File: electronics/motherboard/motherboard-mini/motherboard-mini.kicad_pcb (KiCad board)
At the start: 2 copper layers, 106.6 x 156.6 mm, 167 parts, among them J1 JTAG, J10 CONUFL001-SMD-T, J11 SIM8060-6-0-14-00-A, J12 JTAG, J2 ST1W008S4AR1500, J3 3020-14-0300-00, J5 USB4070-30-C_REVC5, J8 SOLAR_CONN, Q1 MMDT3904, Q2 BC847, Q3 BSS214NW, Q4 BC847, Q5 BC847, SW1 BOOT, SW2 RESET, SW3 PROG_BTN, SW4 CAT_M1_RST, U1 CP2102N-Axx-xQFN28, U10 TPS22967DSGR, U11 SARA-R410M-02B, U12 AOZ8904CIL, U13 TXB0104PW, U14 TCA9534, U2 ESP32-WROOM-32E_(16MB), U3 INA219BxD, U4 LT3652IMSE, U5 MCP73832-2-OT, U6 INA219BxD, U7 MIC2288YD5-TR, U8 XC6215B332MR-G, U9 NCP718xSN500, Y1 32.768KHz

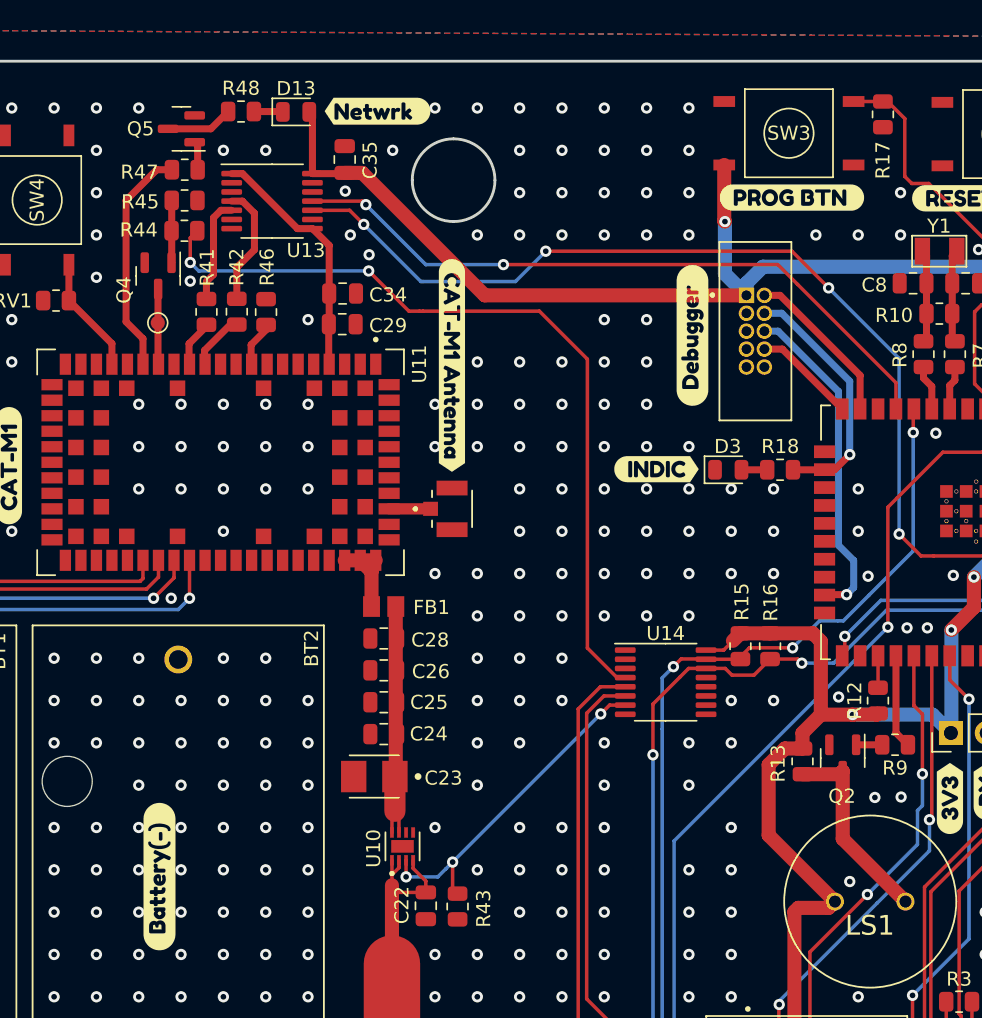
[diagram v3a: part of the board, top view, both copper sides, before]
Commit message: added cat-m1 basic interface
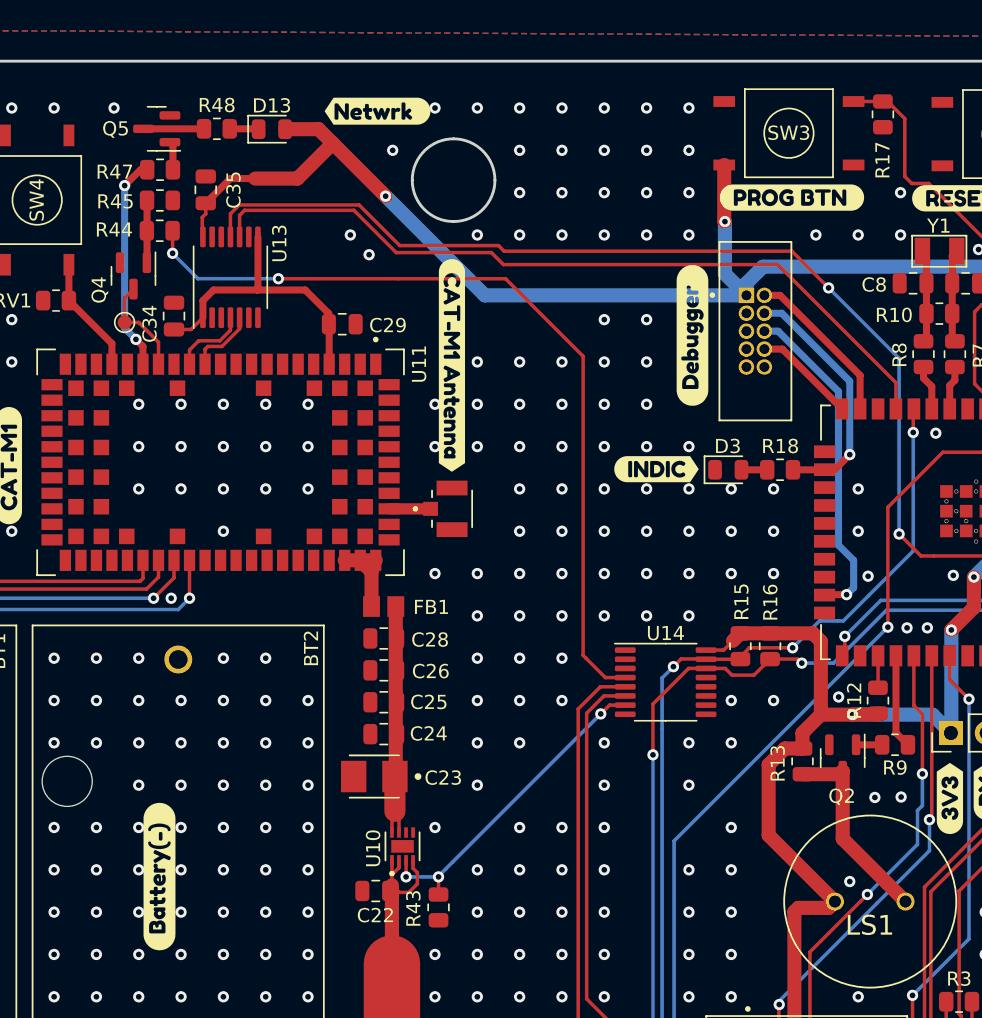
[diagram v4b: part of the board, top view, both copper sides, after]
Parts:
- removed R41, R42, R46: 0, Resistor_SMD:R_0805_2012Metric
- R28: value 27K -> 10K
- R29: value 53.6K -> 21K
- R39: value 43.3K -> 47K
- R40: value 5K -> 4.7K
- moved C34 12.1 mm to (65.5, 44.8), turned to 90 degrees
- moved C35 10.1 mm to (67.8, 35.8)
- moved U13 6.15 mm to (69.5, 42.0), turned to 90 degrees
- moved C22 3.70 mm to (79.8, 85.5), turned to 180 degrees
- moved TP4 2.35 mm to (62.0, 45.2)
- moved D13 2.11 mm to (72.4, 31.5)
- moved R48 2.11 mm to (68.5, 31.5)
- moved Q4 1.75 mm to (62.6, 41.9)
- moved Q5 1.75 mm to (64.3, 31.5)
- moved R44 1.75 mm to (64.5, 38.7)
- moved R45 1.75 mm to (64.5, 36.5)
- moved R47 1.75 mm to (64.5, 34.4)
- moved R43 1.35 mm to (84.2, 86.7)
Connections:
- U11 pad 12: Net-(R42-Pad2) -> TX_1V8
- U11 pad 13: Net-(R41-Pad2) -> RX_1V8
- U11 pad 9: Net-(R46-Pad2) -> GND
- U13 pad 10: UART_TX1 -> UART_RX1
- U13 pad 11: UART_RX1 -> UART_TX1
- U13 pad 4: TX_1V8 -> RX_1V8
- U13 pad 5: RX_1V8 -> TX_1V8
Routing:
- net +3.3V: track 393.7 -> 405.6 mm, vias 14 -> 15
- net UART_RX1: track 48.6 -> 55.1 mm, vias 2 -> 0
- net UART_TX1: track 75.5 -> 81.6 mm, vias 4 -> 2
- net Net-(R42-Pad2): track 3.91 -> 0.00 mm
- net TX_1V8: track 8.56 -> 4.90 mm
- net +1V8: track 17.3 -> 20.9 mm
- net Net-(R41-Pad2): track 3.20 -> 0.00 mm
- net Net-(R46-Pad2): track 3.11 -> 0.00 mm
- net RX_1V8: track 7.47 -> 5.38 mm
- net Net-(Q4-Pad3): track 5.22 -> 7.16 mm
- net VBAT: track 207.4 -> 206.2 mm
- net IO_P3: track 24.1 -> 23.0 mm
- net IO_P0: track 57.5 -> 58.6 mm
- net NETWORK_INDIC: track 16.3 -> 15.3 mm, vias 0 -> 2
- net GND: vias 886 -> 877

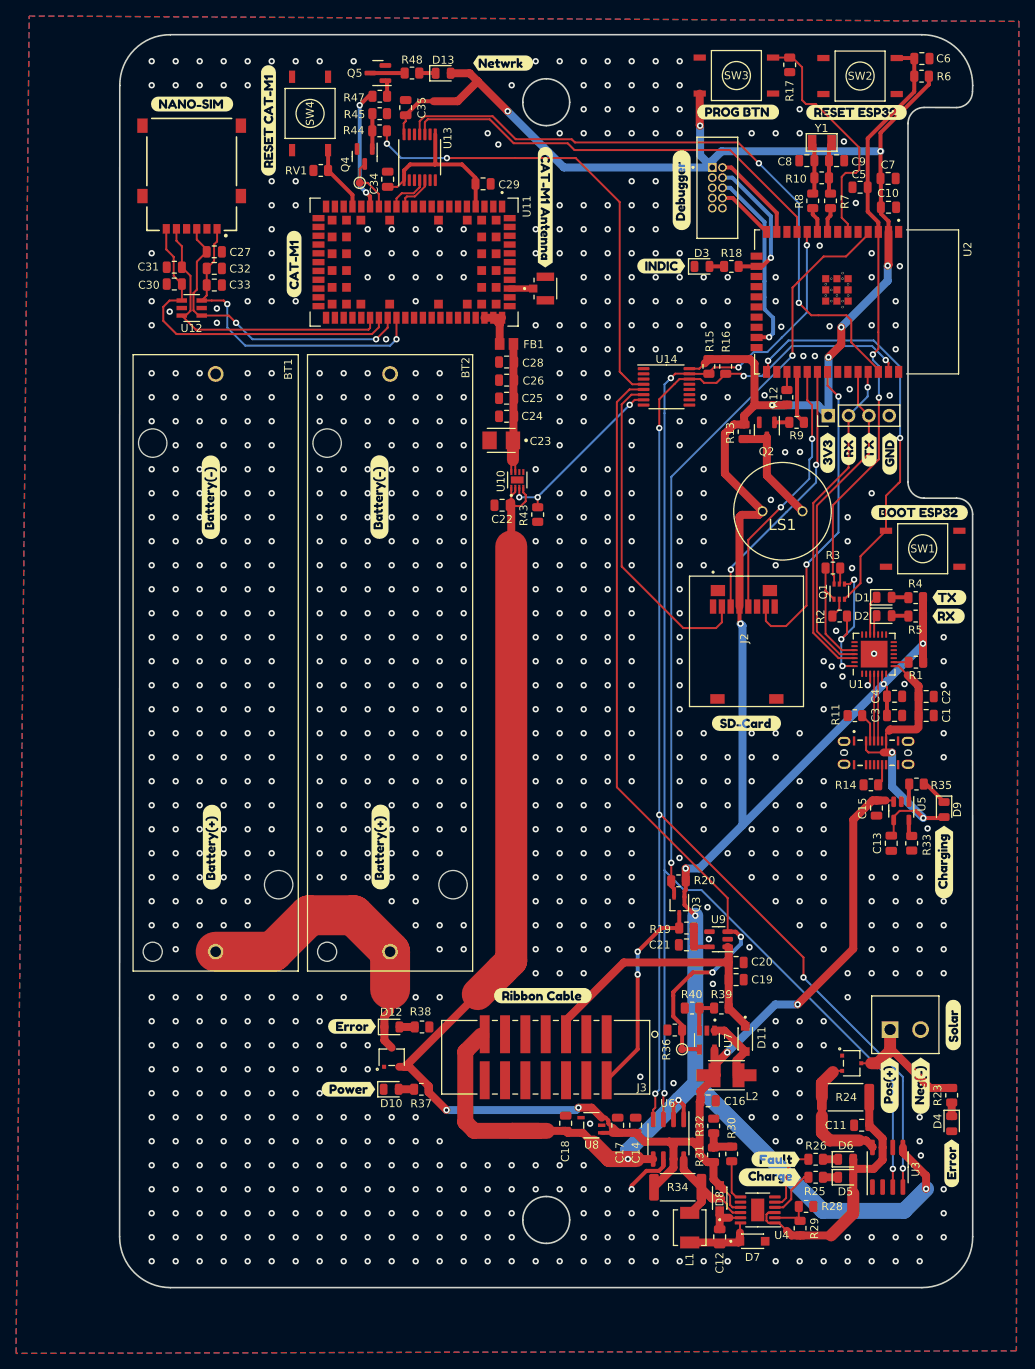
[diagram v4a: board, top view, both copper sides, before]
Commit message: new board version sent for production, termed 'wombat' and breakout board
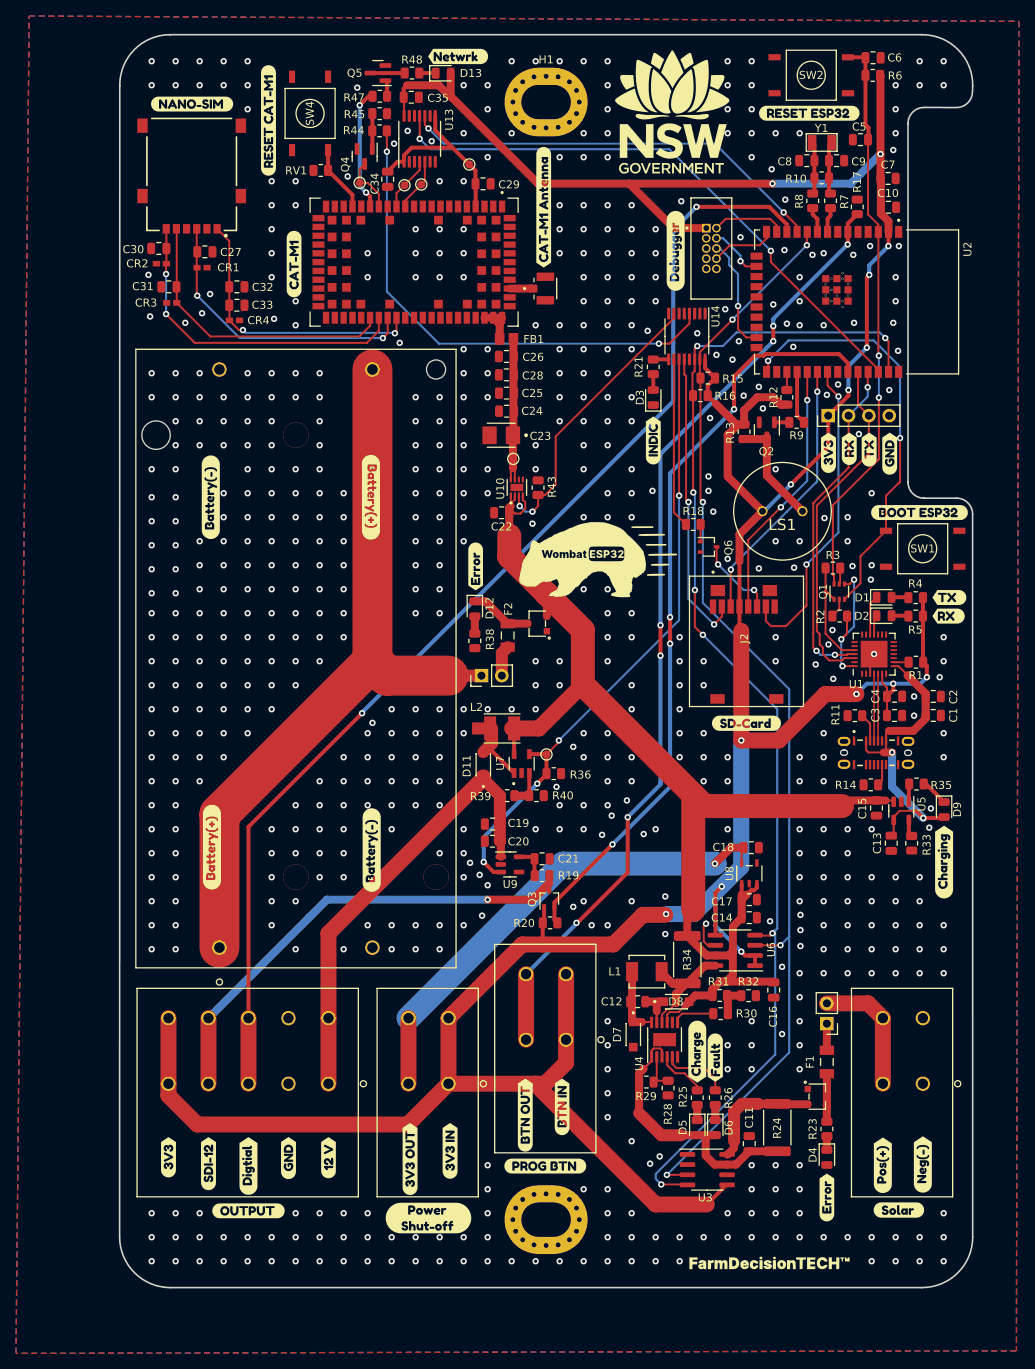
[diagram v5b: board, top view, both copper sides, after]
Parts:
- removed BT1, BT2: 1043, 1043:BAT_1043
- removed D10: LED(Green), LED_SMD:LED_0805_2012Metric
- removed R37: 4.7K, Resistor_SMD:R_0805_2012Metric
- removed SW3: PROG_BTN, 1977223-6:1977223-6
- removed U12: AOZ8904CIL, AOZ8904CIL:AOZ8904CIL
- removed kibuzzard-63606D99: G***, kibuzzard-63606D99
- removed kibuzzard-6361FE78: G***, kibuzzard-6361FE78
- removed kibuzzard-63643CAA: G***, kibuzzard-63643CAA
- removed kibuzzard-6364627B: G***, kibuzzard-6364627B
- removed kibuzzard-636462B0: G***, kibuzzard-636462B0
- removed kibuzzard-63646461: G***, kibuzzard-63646461
- added B1: 1049P, 1049P:1049P, F.Cu at (44.5, 140.8)
- added CR1: PESD0402-140, PESD0402-140:PESD0402-140, F.Cu at (42.3, 55.8)
- added CR2: PESD0402-140, PESD0402-140:PESD0402-140, F.Cu at (37.2, 55.3)
- added CR3: PESD0402-140, PESD0402-140:PESD0402-140, F.Cu at (38.5, 60.2)
- added CR4: PESD0402-140, PESD0402-140:PESD0402-140, F.Cu at (46.4, 62.4)
- added F1: 0685P2000-01, 0685P2000-01:0685P2000-01, F.Cu at (120.4, 155.1)
- added F2: 0685P2000-01, 0685P2000-01:0685P2000-01, F.Cu at (80.5, 101.8)
- added G***: LOGO, LOGO, F.Cu at (91.7, 92.5)
- added G***: LOGO, LOGO, F.Cu at (113.2, 180.2)
- added G***: LOGO, LOGO, F.Cu at (101.3, 36.7)
- added H1: MountingHole, MountingHole:MountingHole_4.3x6.2mm_M4_Pad_Via, F.Cu at (85.3, 35.1)
- added H2: MountingHole, MountingHole:MountingHole_4.3x6.2mm_M4_Pad_Via, F.Cu at (85.3, 174.8)
- added J4: 2604-3105, 2604-3105:2604-3105, F.Cu at (58.1, 157.8)
- added J6: 2604-3102, 2604-3102:2604-3102, F.Cu at (132.4, 157.8)
- added J7: SOLAR_CRNT_JMPR, Connector_PinHeader_2.54mm:PinHeader_1x02_P2.54mm_Vertical, F.Cu at (120.4, 150.3)
- added J9: 2604-3102, 2604-3102:2604-3102, F.Cu at (73.1, 157.8)
- added Q6: BSS214NW, Package_TO_SOT_SMD:SOT-323_SC-70, F.Cu at (105.6, 90.7)
- added R21: 1.2K, Resistor_SMD:R_0805_2012Metric, F.Cu at (98.7, 68.2)
- added TP2: RX_1V8, TestPoint:TestPoint_Pad_D1.0mm, F.Cu at (67.6, 45.5)
- added TP3: TX_1V8, TestPoint:TestPoint_Pad_D1.0mm, F.Cu at (69.7, 45.4)
- added TP5: VOUT, TestPoint:TestPoint_Pad_D1.0mm, F.Cu at (81.2, 79.7)
- added TP6: 1V8, TestPoint:TestPoint_Pad_D1.0mm, F.Cu at (75.7, 42.9)
- added kibuzzard-635F8A75: G***, kibuzzard-635F8A75, F.Cu at (38.1, 167.0)
- added kibuzzard-635F8A8D: G***, kibuzzard-635F8A8D, F.Cu at (53.1, 167.1)
- added kibuzzard-63744C1F: G***, kibuzzard-63744C1F, F.Cu at (85.0, 48.2)
- added kibuzzard-637470B7: G***, kibuzzard-637470B7, F.Cu at (104.2, 153.8)
- added kibuzzard-637470C3: G***, kibuzzard-637470C3, F.Cu at (106.5, 154.6)
- added kibuzzard-63747569: G***, kibuzzard-63747569, F.Cu at (70.6, 174.6)
- added kibuzzard-63747585: G***, kibuzzard-63747585, F.Cu at (48.1, 173.7)
- added kibuzzard-63747865: G***, kibuzzard-63747865, F.Cu at (73.3, 166.2)
- added kibuzzard-63747876: G***, kibuzzard-63747876, F.Cu at (68.3, 167.2)
- added kibuzzard-637478F4: G***, kibuzzard-637478F4, F.Cu at (76.5, 93.2)
- added kibuzzard-6374791F: G***, kibuzzard-6374791F, F.Cu at (43.1, 167.8)
- added kibuzzard-63747928: G***, kibuzzard-63747928, F.Cu at (48.1, 168.1)
- added kibuzzard-63747933: G***, kibuzzard-63747933, F.Cu at (58.1, 167.1)
- added kibuzzard-6374797E: G***, kibuzzard-6374797E, F.Cu at (82.7, 161.7)
- added kibuzzard-6374798A: G***, kibuzzard-6374798A, F.Cu at (87.3, 160.7)
- C24, C29, C33: value 100nF -> 0.1uF
- J3: value 3020-14-0300-00 -> 2604-3102; footprint 3020-14-0300-00:3020-14-0300-00 -> 2604-3102:2604-3102
- J8: value SOLAR_CONN -> BAT_CRNT_JMPR; footprint TBP02R2-381-02BE:CUI_TBP02R2-381-02BE -> Connector_PinHeader_2.54mm:PinHeader_1x02_P2.54mm_Vertical
- R18: value 2K -> 10K
- R38: value 4.7K -> 1.5K
- moved kibuzzard-6360A408 133.9 mm to (85.2, 168.1)
- moved J8 67.6 mm to (77.2, 106.8), turned to 90 degrees
- moved MOSFET2 57.2 mm to (84.2, 100.3), turned to 90 degrees
- moved D12 53.3 mm to (76.4, 98.5), turned to -90 degrees
- moved L2 51.6 mm to (79.8, 113.4), turned to 180 degrees
- moved R38 48.7 mm to (76.4, 102.5), turned to -90 degrees
- moved D11 47.4 mm to (77.5, 117.9), turned to 90 degrees
- moved kibuzzard-635F8E2B 44.1 mm to (63.5, 128.6)
- moved kibuzzard-635F8E59 43.7 mm to (63.4, 84.5), turned to -90 degrees
- moved U7 41.6 mm to (82.2, 117.8), turned to 90 degrees
- moved C18 41.5 mm to (111.0, 128.3), turned to 0 degrees
- moved TP1 40.6 mm to (85.3, 116.7), turned to 180 degrees
- moved R39 37.7 mm to (80.4, 121.8), turned to 180 degrees
- moved U8 37.2 mm to (110.7, 131.5), turned to 90 degrees
- moved C19 36.1 mm to (78.6, 125.3), turned to 180 degrees
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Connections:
- C18 pad 1: +3.3V -> Net-(C18-Pad1)
- J2 pad 6: GND -> Net-(Q6-Pad3)
- J3 pad 1: unconnected-(J3-Pad1) -> +3.3V
- J3 pad 2: SDI12_IN_OUT -> +3.3V
- J3 pad 3: GND -> GPIO34
- J3 pad 4: GND -> GPIO34
- J8 pad 1: Net-(J8-Pad1) -> Net-(B1-Pad1)
- J8 pad 2: GND -> Net-(F2-Pad2)
- MOSFET1 pad 3: Net-(J8-Pad1) -> Net-(R23-Pad1)
- Q3 pad 2: GPIO36 -> GPIO21
- R18 pad 1: GPIO13 -> IO_P5
- R18 pad 2: Net-(D3-Pad2) -> Net-(Q6-Pad1)
- R20 pad 2: GPIO36 -> GPIO21
- R23 pad 1: Net-(J8-Pad1) -> Net-(R23-Pad1)
- U1 pad 25: UART_TX0 -> UART_RX0
- U1 pad 26: UART_RX0 -> UART_TX0
- U14 pad 10: unconnected-(U14-Pad10) -> IO_P5
- U14 pad 11: unconnected-(U14-Pad11) -> IO_P1
- U14 pad 12: unconnected-(U14-Pad12) -> IO_P2
- U14 pad 13: GPIO21 -> unconnected-(U14-Pad13)
- U14 pad 5: IO_P1 -> unconnected-(U14-Pad5)
- U14 pad 6: IO_P2 -> unconnected-(U14-Pad6)
- U14 pad 9: IO_P4 -> Net-(U14-Pad9)
- U2 pad 12: unconnected-(U2-Pad12) -> GPIO27
- U2 pad 33: unconnected-(U2-Pad33) -> GPIO21
- U2 pad 4: GPIO36 -> unconnected-(U2-Pad4)
- U8 pad 5: +3.3V -> Net-(C18-Pad1)
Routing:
- net GPIO27: track 0.00 -> 145.9 mm, vias 0 -> 2
- net GPIO36: track 95.1 -> 0.00 mm, vias 2 -> 0
- net GPIO21: track 0.00 -> 94.7 mm, vias 0 -> 4
- net Net-(B1-Pad1): track 0.00 -> 94.6 mm
- net GPIO34: track 30.4 -> 120.4 mm, vias 0 -> 7
- net Net-(C18-Pad1): track 0.00 -> 61.0 mm, vias 0 -> 1
- net VBAT: track 206.2 -> 154.0 mm, vias 4 -> 0
- net +3.3V: track 405.6 -> 453.5 mm, vias 15 -> 14
- net I2C_SDA: track 176.3 -> 141.7 mm
- net SDI12_IN_OUT: track 26.0 -> 59.7 mm, vias 2 -> 1
- net I2C_SCL: track 183.7 -> 151.3 mm
- net Net-(D12-Pad1): track 38.2 -> 7.77 mm
- net IO_P1: track 99.5 -> 77.8 mm, vias 2 -> 4
- net IO_P5: track 0.00 -> 21.3 mm
- net +12V: track 35.9 -> 57.2 mm
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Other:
- outline, holes or cut-outs redrawn
